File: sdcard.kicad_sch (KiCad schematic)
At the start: 24 parts, among them J9 microSD push-pull, Q6 DMG2301L, Q7 2N7002, U10 SRV05-4, U11 SRV05-4

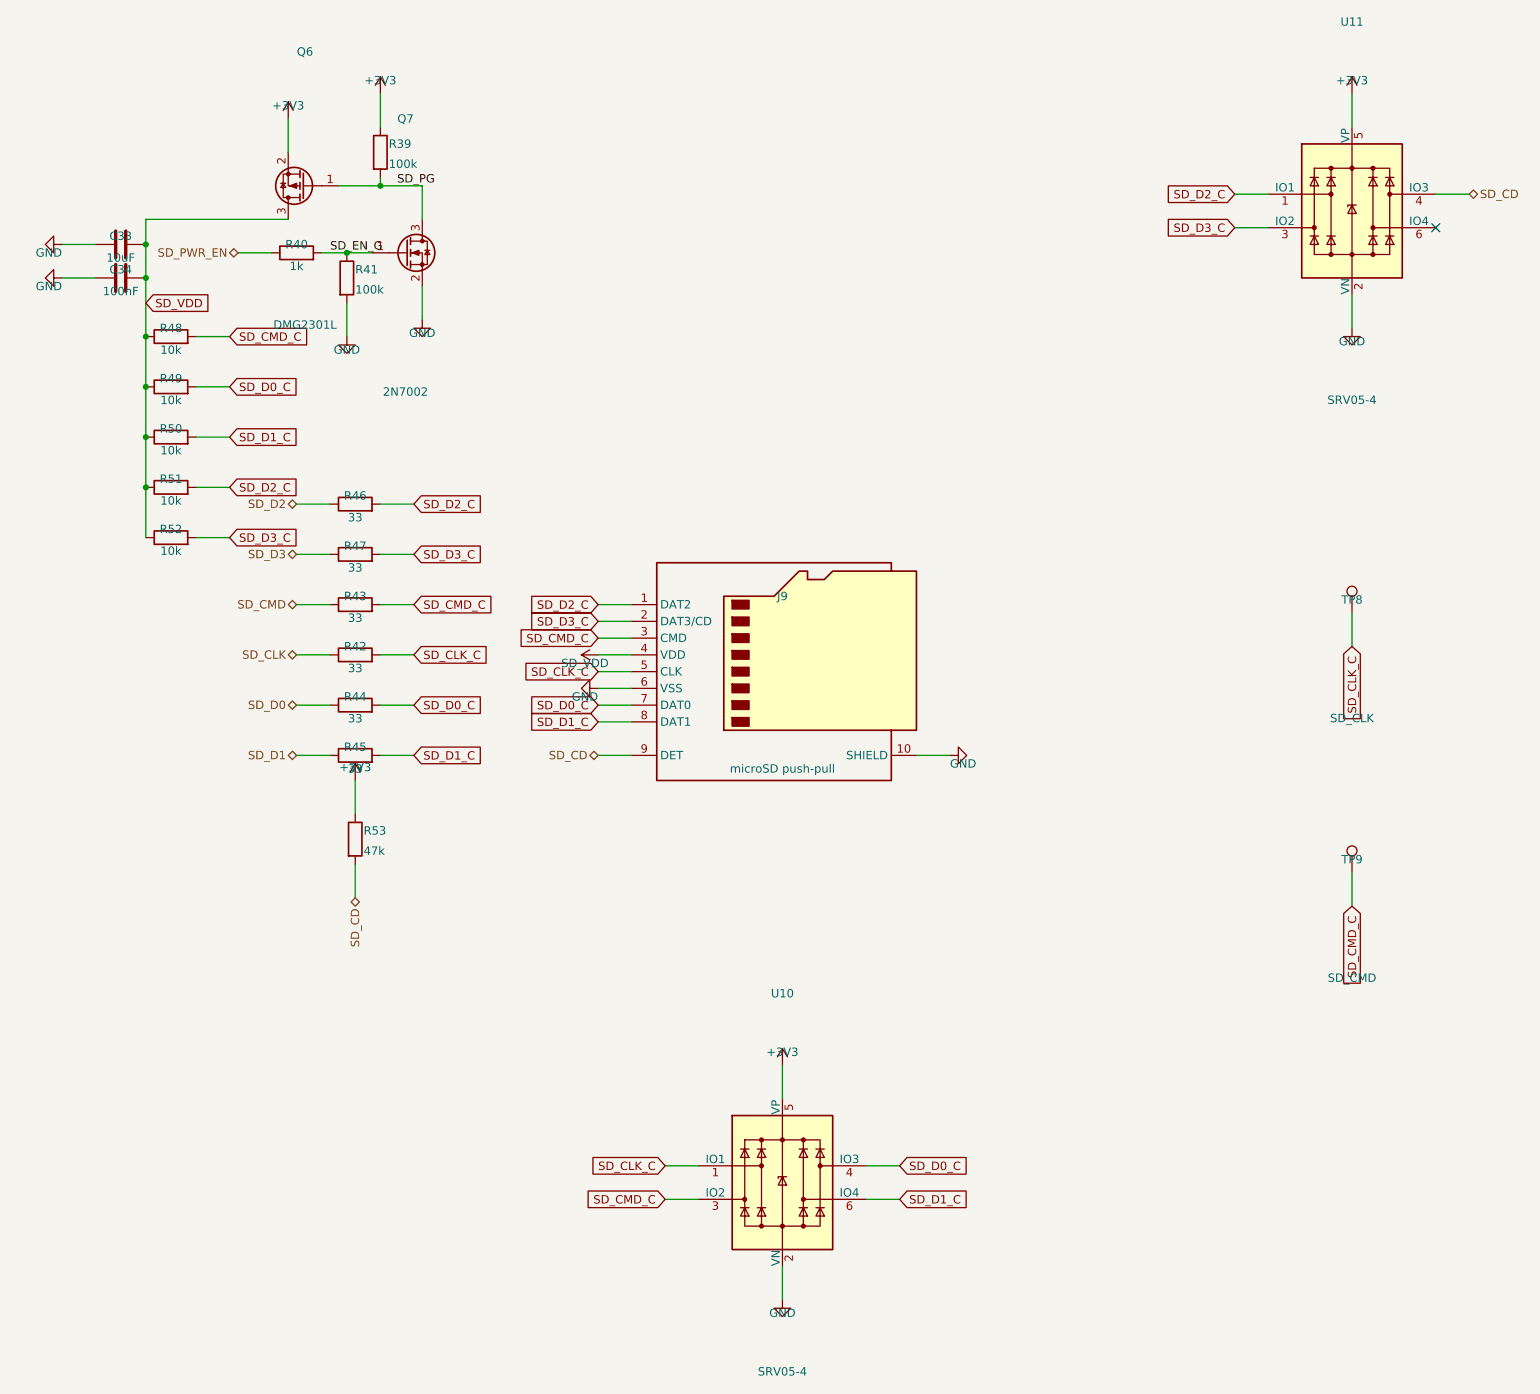
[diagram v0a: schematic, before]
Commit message: Re-scope the fork as a carrier board: no power section, differential analog, K-line
The shield idea does not survive measurement. Component courtyard on the
parent is 3052 mm2 over an 84 x 100 board -- 36% packing, not the 50% I had
been estimating -- and a DevKitC-1 is 63 x 25.5 = 1607 mm2. The parts alone
were 1.4x the whole dev board. So this is a carrier the dev board plugs into,
not a shield that fits on top of one.

Power section deleted entirely. It was 1746 mm2, 57% of the board, for two
rails the DevKitC-1 already makes from its USB-C. Gone: both LM5164 bucks and
everything around them, the LM74700 ideal diode, the reverse-battery FET, the
three electrolytic cans, the 12 V input, and the sensor-rail load switch.
Both rails are now inputs, taken up through the sockets -- which reverses the
earlier "feed 5 V only" rule, because there is no longer a second regulator
to parallel against.

Hold-up is a supercapacitor, not electrolytics. The first sizing was wrong:
energy goes as V-squared and the usable window at 5 V is 4.2 -> 3.6 V, so
2000 uF buys 12.5 ms, not the ~50 ms claimed. 0.5 F over the same window is
2.5 s, in less area than one of the 100 V cans it replaces. Low-ESR
cylindrical cells specifically -- coin EDLCs are 30-200 ohm and cannot source
120 mA at all.

Analog runs differentially. The board is grounded twice now, through the
sensor loom and through USB by way of a charger elsewhere in the car, and a
few hundred mV of chassis drop is 6% of a 0-5 V channel -- which makes the
0.1% dividers pointless. The correction has to be at the divider, not the
ADC, so the sensor ground comes back as a Kelvin wire through a matched
attenuator. Two ADS1115s, because one MUX only offers three channels against
a shared negative.

K-line added, discrete rather than an L9637D: that part's TXD threshold is
0.7*VCC = 3.5 V and a 3.3 V GPIO cannot meet it. Low-side 2N7002, clamped
22k/10k receiver, optional ISO 9141 tester pull-up on a jumper.

Pin map regrouped by boa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
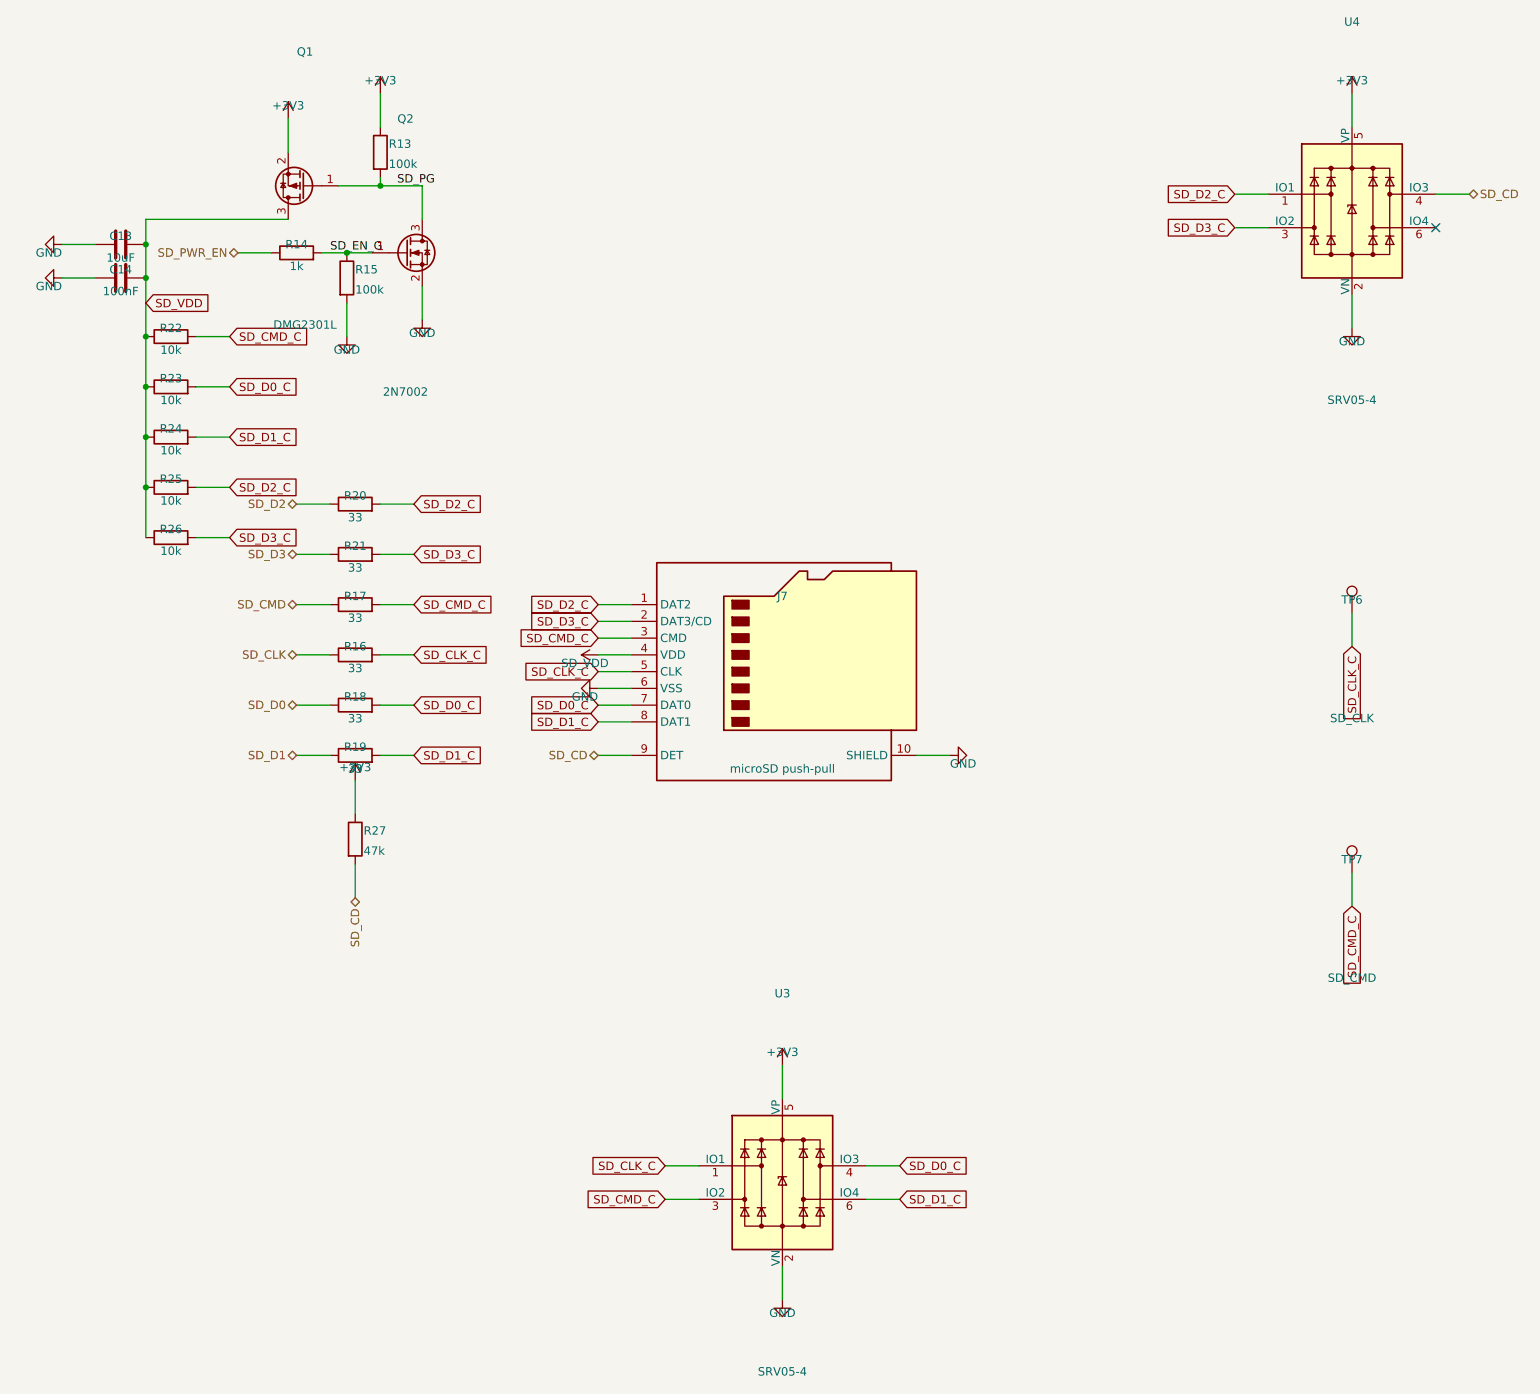
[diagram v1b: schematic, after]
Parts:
- removed C33: 10uF, Capacitor_SMD:C_1206_3216Metric, symbol Device:C
- removed C34: 100nF, Capacitor_SMD:C_0805_2012Metric, symbol Device:C
- removed J9: microSD push-pull, Connector_Card:microSD_HC_Hirose_DM3D-SF, symbol Connector:Micro_SD_Card_Det1
- removed Q6: DMG2301L, Package_TO_SOT_SMD:SOT-23, symbol Transistor_FET:Q_PMOS_GSD
- removed Q7: 2N7002, Package_TO_SOT_SMD:SOT-23, symbol Transistor_FET:Q_NMOS_GSD
- removed R39, R41: 100k, Resistor_SMD:R_0805_2012Metric, symbol Device:R
- removed R40: 1k, Resistor_SMD:R_0805_2012Metric, symbol Device:R
- removed R42, R43, R44, R45, R46, R47: 33, Resistor_SMD:R_0805_2012Metric, symbol Device:R
- removed R48, R49, R50, R51, R52: 10k, Resistor_SMD:R_0805_2012Metric, symbol Device:R
- removed R53: 47k, Resistor_SMD:R_0805_2012Metric, symbol Device:R
- removed TP8: SD_CLK, TestPoint:TestPoint_Pad_D1.5mm, symbol Connector:TestPoint
- removed TP9: SD_CMD, TestPoint:TestPoint_Pad_D1.5mm, symbol Connector:TestPoint
- removed U10, U11: SRV05-4, Package_TO_SOT_SMD:SOT-23-6, symbol Power_Protection:SRV05-4
- added C13: 10uF, Capacitor_SMD:C_1206_3216Metric, symbol Device:C
- added C14: 100nF, Capacitor_SMD:C_0805_2012Metric, symbol Device:C
- added J7: microSD push-pull, Connector_Card:microSD_HC_Hirose_DM3D-SF, symbol Connector:Micro_SD_Card_Det1
- added Q1: DMG2301L, Package_TO_SOT_SMD:SOT-23, symbol Transistor_FET:Q_PMOS_GSD
- added Q2: 2N7002, Package_TO_SOT_SMD:SOT-23, symbol Transistor_FET:Q_NMOS_GSD
- added R13, R15: 100k, Resistor_SMD:R_0805_2012Metric, symbol Device:R
- added R14: 1k, Resistor_SMD:R_0805_2012Metric, symbol Device:R
- added R16, R17, R18, R19, R20, R21: 33, Resistor_SMD:R_0805_2012Metric, symbol Device:R
- added R22, R23, R24, R25, R26: 10k, Resistor_SMD:R_0805_2012Metric, symbol Device:R
- added R27: 47k, Resistor_SMD:R_0805_2012Metric, symbol Device:R
- added TP6: SD_CLK, TestPoint:TestPoint_Pad_D1.5mm, symbol Connector:TestPoint
- added TP7: SD_CMD, TestPoint:TestPoint_Pad_D1.5mm, symbol Connector:TestPoint
- added U3, U4: SRV05-4, Package_TO_SOT_SMD:SOT-23-6, symbol Power_Protection:SRV05-4
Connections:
- net +3V3: now also Q1.2 (S), R13.1, R27.1, U3.5 (VP), U4.5 (VP)
- net GND: now also C13.2, C14.2, J7.10 (SHIELD), J7.6 (VSS), Q2.2 (S), R15.2, U3.2 (VN), U4.2 (VN)
- net SD_CD: now also J7.9 (DET), R27.2, U4.4 (IO3)
- net SD_CLK: now also R16.1
- net SD_CLK_C: now also J7.5 (CLK), R16.2, TP6.1, U3.1 (IO1)
- net SD_CMD: now also R17.1
- net SD_CMD_C: now also J7.3 (CMD), R17.2, R22.2, TP7.1, U3.3 (IO2)
- net SD_D0: now also R18.1
- net SD_D0_C: now also J7.7 (DAT0), R18.2, R23.2, U3.4 (IO3)
- net SD_D1: now also R19.1
- net SD_D1_C: now also J7.8 (DAT1), R19.2, R24.2, U3.6 (IO4)
- net SD_D2: now also R20.1
- net SD_D2_C: now also J7.1 (DAT2), R20.2, R25.2, U4.1 (IO1)
- net SD_D3: now also R21.1
- net SD_D3_C: now also J7.2 (DAT3/CD), R21.2, R26.2, U4.3 (IO2)
- net SD_EN_G: now also Q2.1 (G), R14.2, R15.1
- net SD_PG: now also Q1.1 (G), Q2.3 (D), R13.2
- net SD_PWR_EN: now also R14.1
- net SD_VDD: now also C13.1, C14.1, J7.4 (VDD), Q1.3 (D), R22.1, R23.1, R24.1, R25.1, R26.1

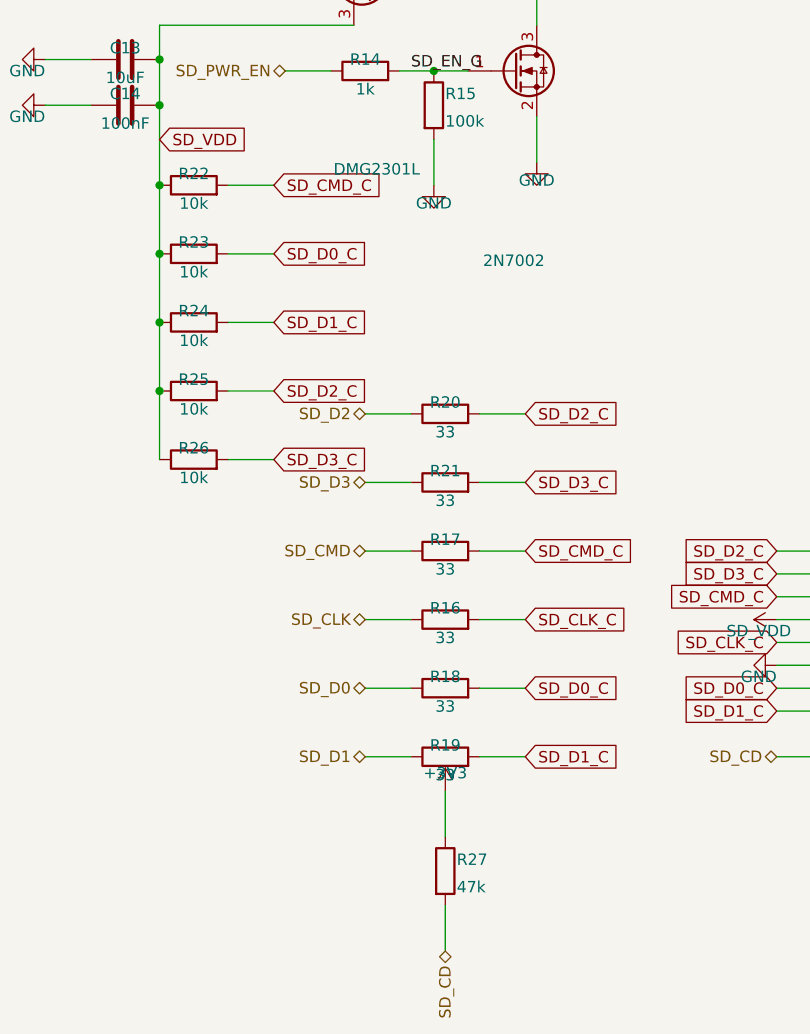
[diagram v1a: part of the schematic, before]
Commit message: Second CAN bus, single analog range, and three placement bugs the render caught
TWO CAN BUSES AT ONCE NEEDS A SECOND CONTROLLER. The ESP32-S3 has exactly
one TWAI peripheral. Two transceivers on it would give a bus you can pick at
runtime through the GPIO matrix, never two live at once, and the point of a
second bus is watching the powertrain and the body bus together. So the
second channel is an MCP2518FD on SPI (SOIC-14, KiCad ships the pin-compatible
MCP2517FD symbol) with its own 40 MHz crystal, its own TJA1051 -- same part
as CAN 1, so two positions on one BOM line -- choke, split termination and
clamps.

That cost five pins against two spare. The three came from dropping the
microSD to 1-bit SDMMC, which measurement says is free: the busiest case this
logger will see is ~128 kB/s against 1-bit's ~1500 kB/s, and bus width does
not touch the card's internal write stall, which is the only thing the
hold-up budget is actually sized around. The card keeps its D1/D2/D3
pull-ups because a card samples DAT3 at power-up and drops into SPI mode if
it finds it low -- they simply stop at the socket now.

Jumpers on the aux harness pins pick K-line or the second CAN pair, because
those two genuinely cannot share a wire: K-line idles at battery voltage and
a CAN transceiver biases its bus to 2.5 V. The clamps sit ahead of the
jumpers so the protection is the same either way, which also let the K-line
drop its own TVS. Default is K-line, which is what an R53 wants.

ANALOG DOWN TO ONE RANGE. The bypass and range-select jumpers are gone --
twelve jumpers and four resistors -- and every channel is a fixed 2.21/13.21
divider spanning 0-16 V, so a 5 V and a 12 V sensor both fit without
touching anything. Resolution was never the reason for a narrower range: a
5 V sensor lands at 0.836 V, which on a 16-bit ADS1115 is 6688 counts.

The real reason is the differential ground. A channel switched to 0-16 V
while the shared return attenuator stayed at the 0-5 V ratio subtracts
0.5769*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
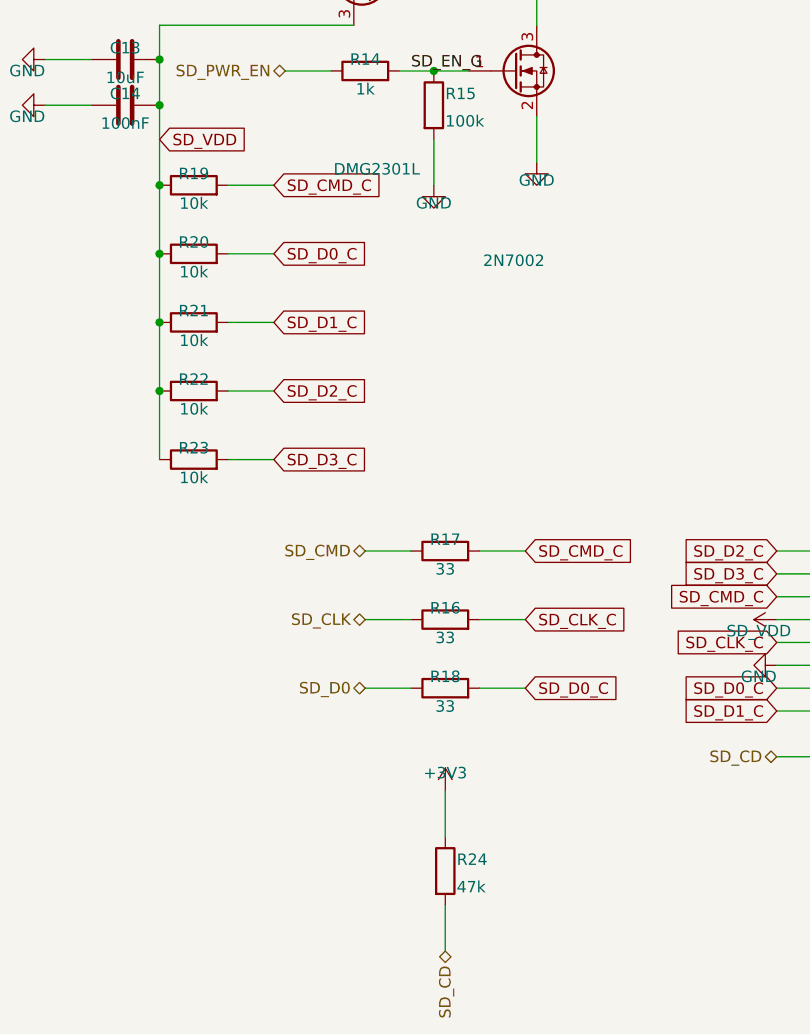
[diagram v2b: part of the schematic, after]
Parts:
- removed R25, R26: 10k, Resistor_SMD:R_0805_2012Metric, symbol Device:R
- removed R27: 47k, Resistor_SMD:R_0805_2012Metric, symbol Device:R
- R19, R20, R21: value 33 -> 10k; Note Series damping -> Espressif's recommended value; pulled to the switched rail 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
- R22, R23: Note Espressif's recommended value; pulled to the switched rail so nothing back-feeds a powered-down card -> Espressif's recommended value; pulled to the switched rail so nothing back-feeds a powered-down card. For D1/D2/D3 this is now the ONLY thing on the net besides the card and its ESD clamp
- R24: value 10k -> 47k; Note Espressif's recommended value; pulled to the switched rail 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 -> Card-detect pull-up
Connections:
- net SD_D1 is gone; now on net SD_VDD: R19.1
- net SD_D2 is gone; now on net SD_VDD: R20.1
- net SD_D3 is gone; now on net SD_VDD: R21.1
- net +3V3: now also R24.1
- net SD_CD: now also R24.2
- net SD_CMD_C: now also R19.2; no longer R22.2
- net SD_D0_C: now also R20.2; no longer R23.2
- net SD_D1_C: now also R21.2; no longer R19.2, R24.2
- net SD_D2_C: now also R22.2; no longer R20.2
- net SD_D3_C: now also R23.2; no longer R21.2
- net SD_VDD: no longer R24.1
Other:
- moved on the sheet: R19, R20, R21, R22, R23, R24
